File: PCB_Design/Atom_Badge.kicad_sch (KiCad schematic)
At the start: 6 parts

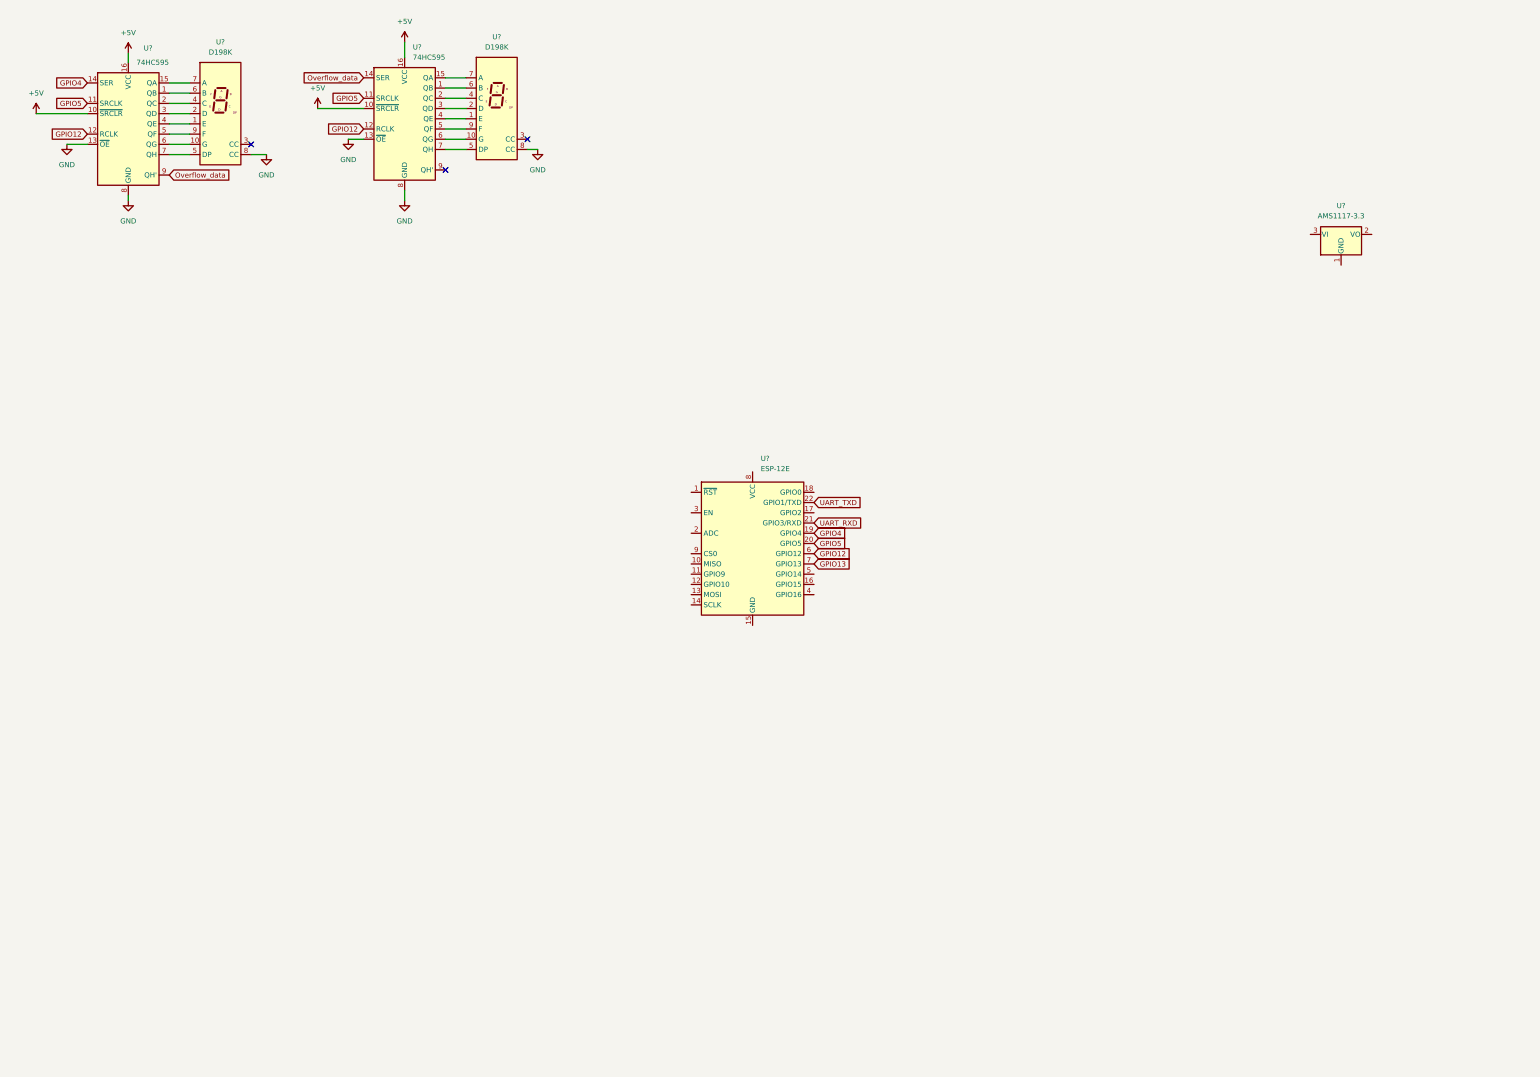
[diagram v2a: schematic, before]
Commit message: added ch340g
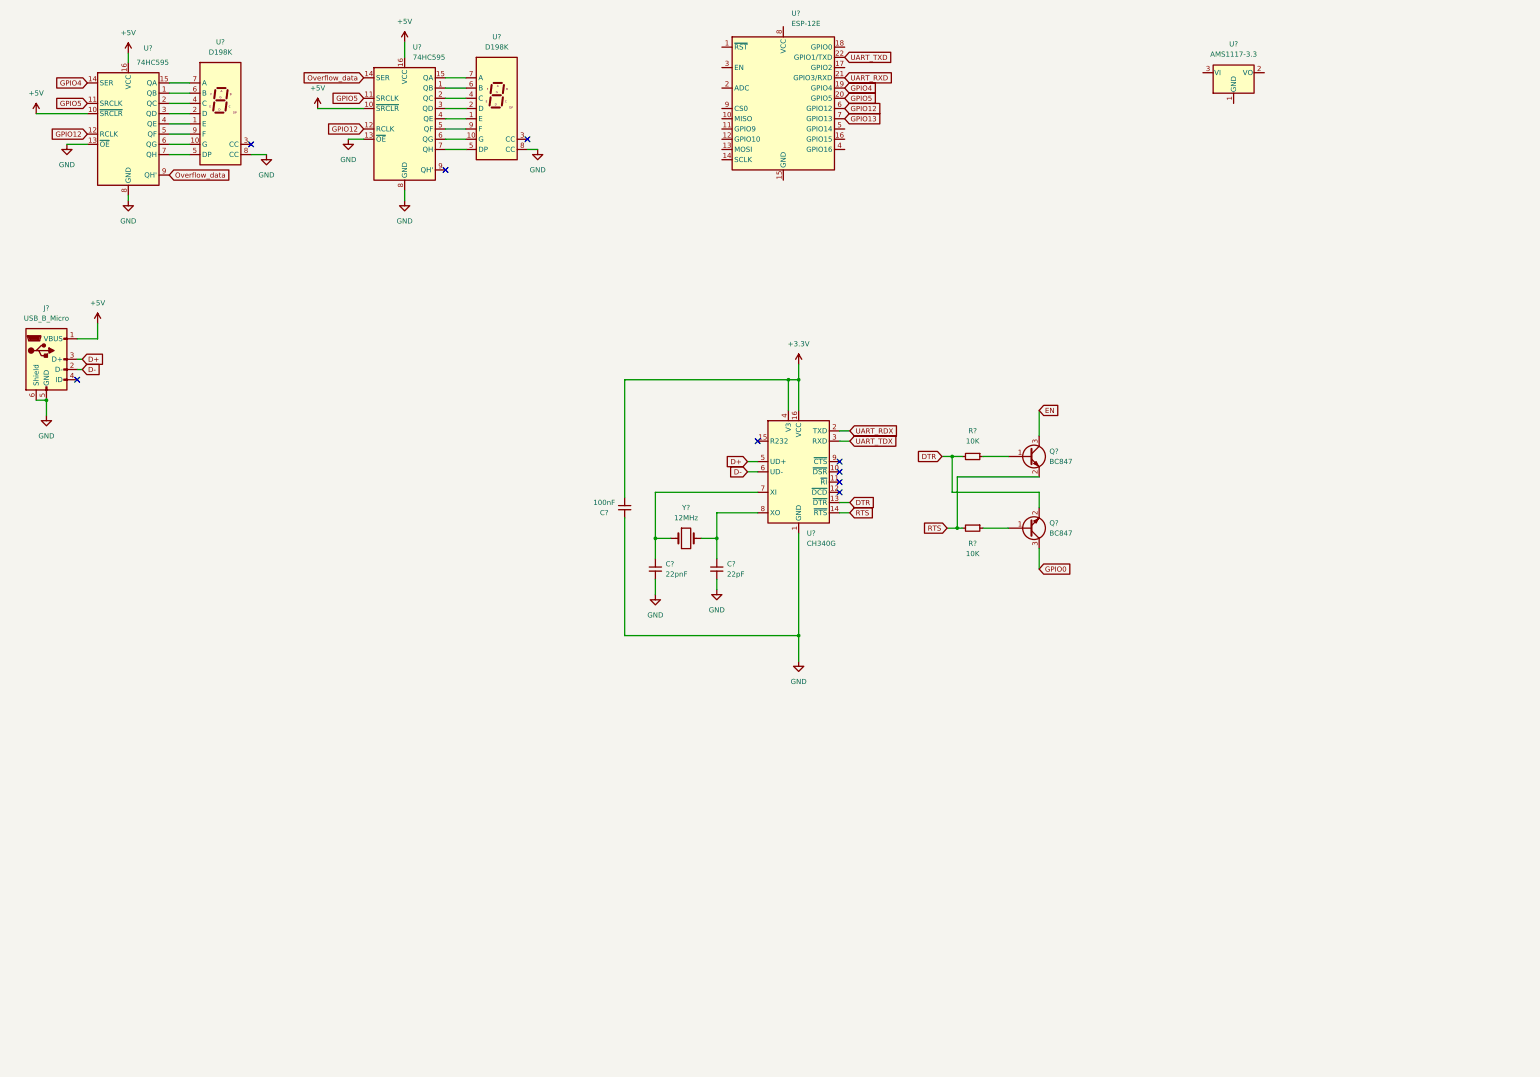
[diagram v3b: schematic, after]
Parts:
- added C?: 22pF, symbol Device:C_Small
- added C?: 100nF, symbol Device:C_Small
- added C?: 22pnF, symbol Device:C_Small
- added J?: USB_B_Micro, symbol Connector:USB_B_Micro
- added Q? (x2): BC847, Package_TO_SOT_SMD:SOT-23, symbol Transistor_BJT:BC847
- added R? (x2): 10K, symbol Device:R_Small
- added U?: CH340G, Package_SO:SOIC-16_3.9x9.9mm_P1.27mm, symbol Interface_USB:CH340G
- added Y?: 12MHz, symbol Device:Crystal
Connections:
- net +5V: now also J?.1 (VBUS)
- net GND: now also C?.2, C?.2, C?.2, J?.5 (GND), J?.6 (Shield), U?.1 (GND)
- new net: Q?.1 (B), R?.1 (x2)
- new net: C?.1, U?.8 (XO), Y?.2
- new net: C?.1, U?.7 (XI), Y?.1
- new net +3V3: C?.1, U?.16 (VCC), U?.4 (V3)
- new net D+: J?.3 (D+), U?.5 (UD+)
- new net D-: J?.2 (D-), U?.6 (UD-)
- new net DTR: Q?.2 (E), R?.2, U?.13 (~{DTR})
- new net EN: Q?.3 (C)
- new net GPIO0: Q?.3 (C)
- new net RTS: Q?.2 (E), R?.2, U?.14 (~{RTS})
- new net UART_RDX: U?.2 (TXD)
- new net UART_TDX: U?.3 (RXD)
- no-connect marks 3 -> 9
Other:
- moved on the sheet: U?

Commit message: Completed 7 segment schematic
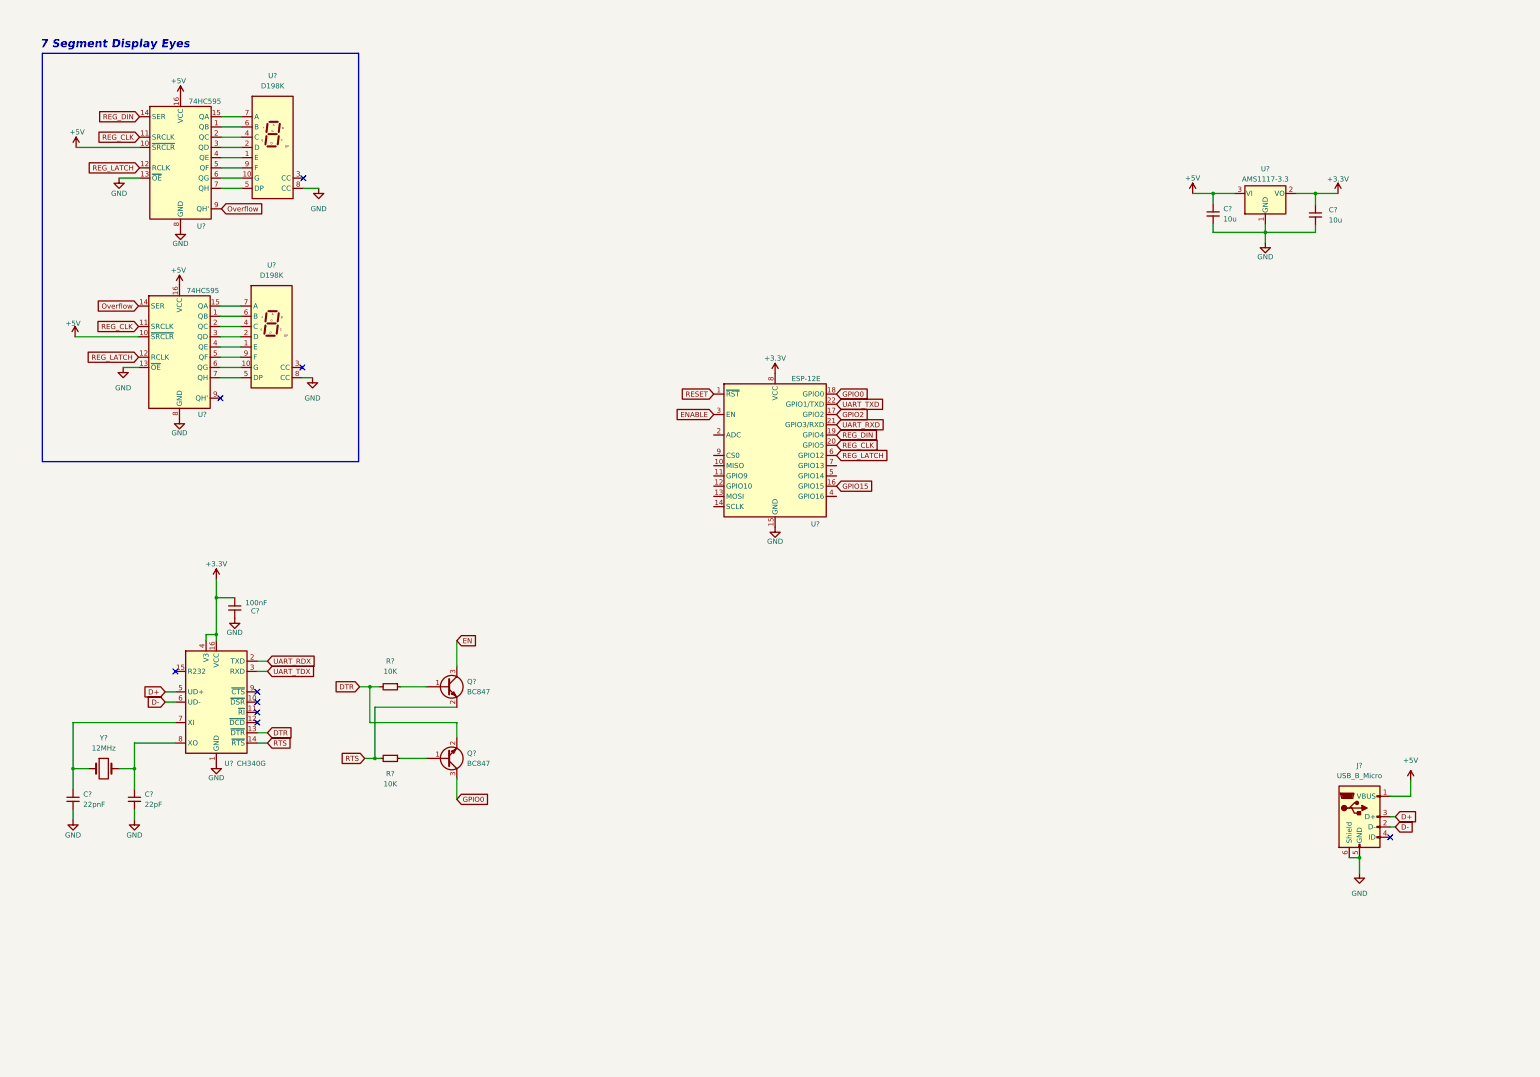
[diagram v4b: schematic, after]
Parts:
- removed C?: 100nF, symbol Device:C_Small
- added C? (x2): 10u, symbol Device:C_Small
- added C?: 100nF, symbol Device:C_Small
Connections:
- net +3V3: now also U?.8 (VCC), C?.1
- net +5V: now also U?.3 (VI), C?.1
- net GND: now also U?.1 (GND), U?.15 (GND), C?.2, C?.2, C?.2
- net GPIO0: now also U?.18 (GPIO0)
- net +3.3V: now reaches U?.2 (VO)
- net +3.3V: now also C?.1
- net RESET: now reaches U?.1 (~{RST})
- net GPIO15: now reaches U?.16 (GPIO15)
- net GPIO2: now reaches U?.17 (GPIO2)
- net ENABLE: now reaches U?.3 (EN)
- net GPIO12 renamed REG_LATCH
- net GPIO13: no longer names the net of U?.7 (GPIO13)
- net GPIO4 renamed REG_DIN
- net GPIO5 renamed REG_CLK
- net Overflow_data renamed Overflow
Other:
- note added: "7 Segment Display Eyes"
- moved on the sheet: C?, J?, Q?, R?, U?, Y?

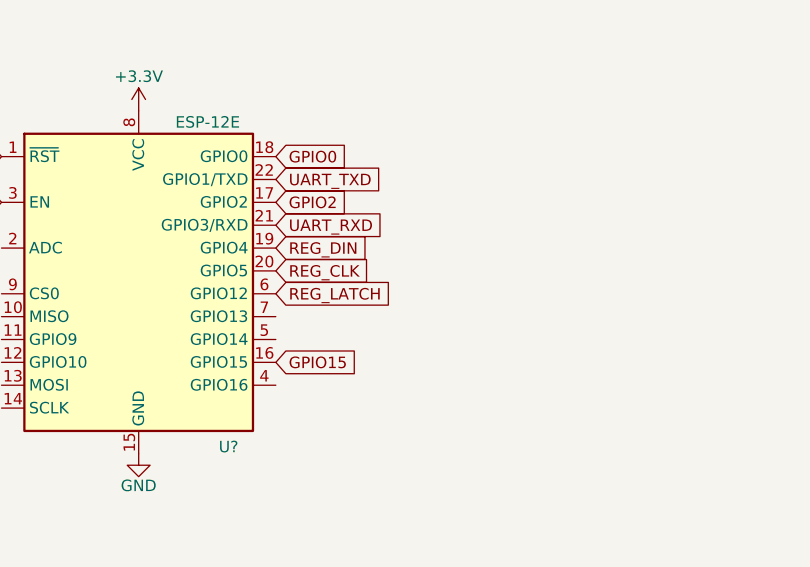
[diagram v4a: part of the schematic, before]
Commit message: Labelled I2C pins
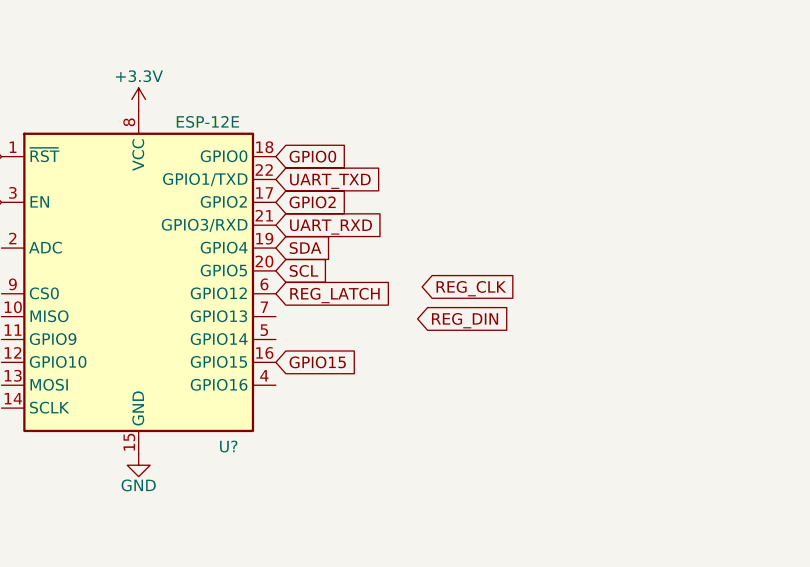
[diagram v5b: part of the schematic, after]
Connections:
- net REG_CLK: no longer U?.20 (GPIO5)
- net REG_DIN: no longer U?.19 (GPIO4)
- new net SCL: U?.20 (GPIO5)
- new net SDA: U?.19 (GPIO4)
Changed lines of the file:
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@@
     (effects (font (size 2 2) (thickness 0.254) bold italic) (justify left bottom))
   )
-  (global_label "REG_DIN" (shape input) (at 222.758 120.396 0) (fields_autoplaced)
+  (global_label "SDA" (shape input) (at 222.758 120.396 0) (fields_autoplaced)
     (effects (font (size 1.27 1.27)) (justify left))
-    (property "Intersheet References" "${INTERSHEET_REFS}" (id 0) (at 233.033 120.4754 0)
+    (property "Intersheet References" "${INTERSHEET_REFS}" (id 0) (at 228.7392 120.3166 0)
+      (effects (font (size 1.27 1.27)) (justify left) hide)
+    )
+  )
+  (global_label "REG_CLK" (shape input) (at 239.014 124.714 0) (fields_autoplaced)
+    (effects (font (size 1.27 1.27)) (justify left))
+    (property "Intersheet References" "${INTERSHEET_REFS}" (id 0) (at 249.6519 124.7934 0)
       (effects (font (size 1.27 1.27)) (justify left) hide)
     )
@@
     (property "Intersheet References" "${INTERSHEET_REFS}" (id 0) (at 182.8497 115.2366 0)
       (effects (font (size 1.27 1.27)) (justify right) hide)
+    )
+  )
+  (global_label "REG_DIN" (shape input) (at 238.506 128.27 0) (fields_autoplaced)
+    (effects (font (size 1.27 1.27)) (justify left))
+    (property "Intersheet References" "${INTERSHEET_REFS}" (id 0) (at 248.781 128.3494 0)
+      (effects (font (size 1.27 1.27)) (justify left) hide)
     )
   )
@@
     )
   )
-  (global_label "REG_CLK" (shape input) (at 222.758 122.936 0) (fields_autoplaced)
+  (global_label "SCL" (shape input) (at 222.758 122.936 0) (fields_autoplaced)
     (effects (font (size 1.27 1.27)) (justify left))
-    (property "Intersheet References" "${INTERSHEET_REFS}" (id 0) (at 233.3959 123.0154 0)
+    (property "Intersheet References" "${INTERSHEET_REFS}" (id 0) (at 228.6787 122.8566 0)
       (effects (font (size 1.27 1.27)) (justify left) hide)
     )

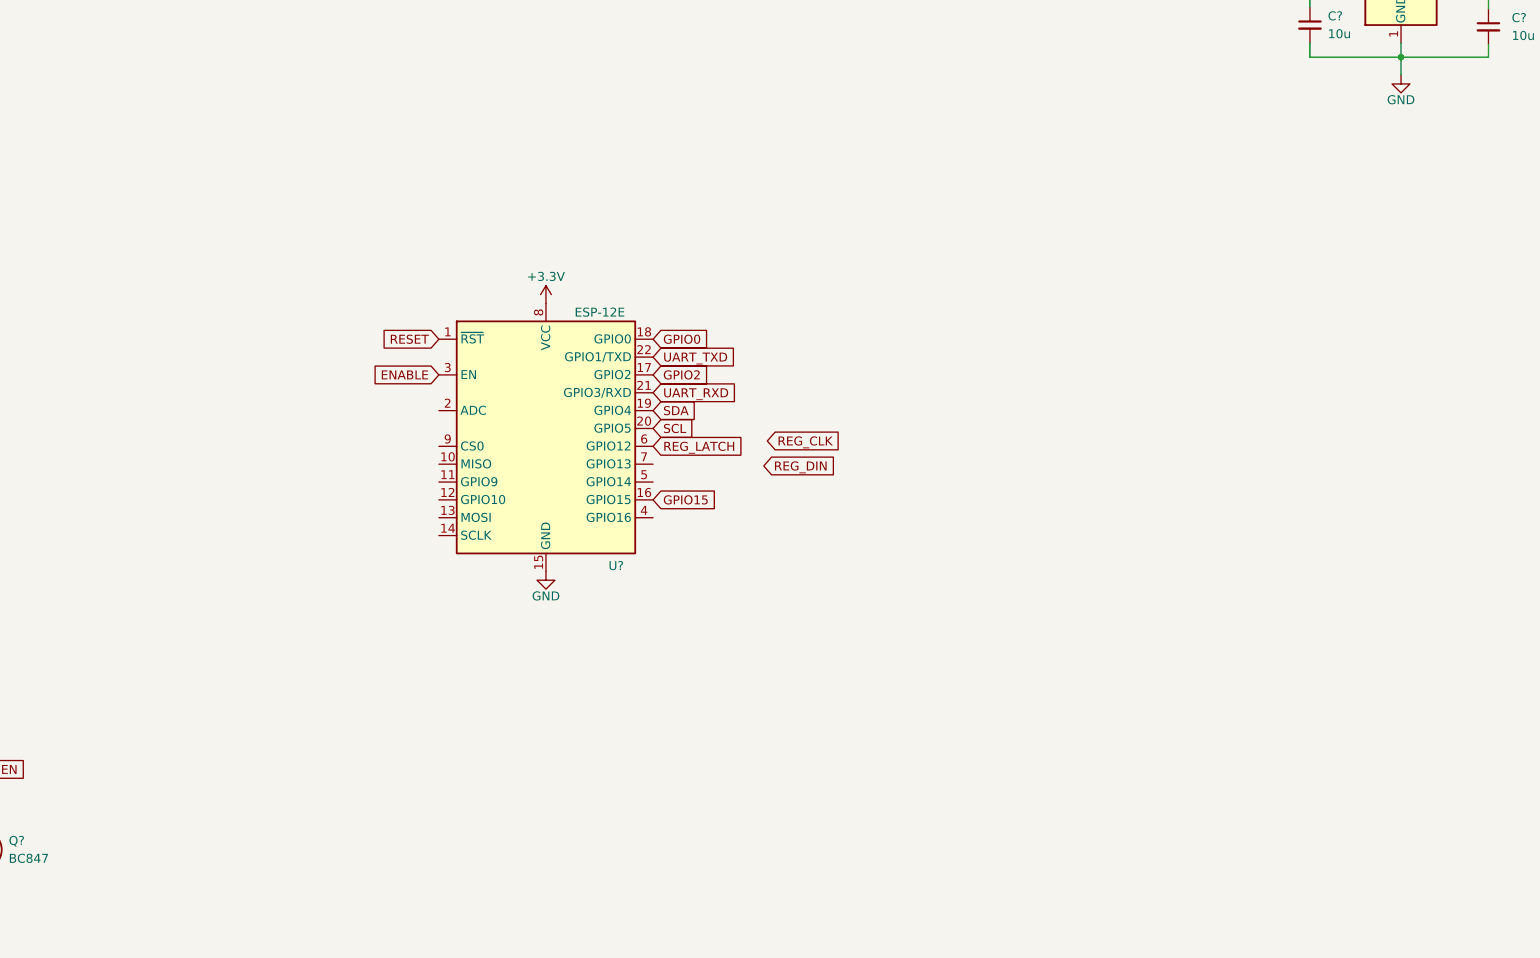
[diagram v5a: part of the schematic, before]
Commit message: transistor model fixed & reset gpio 15 and 2 ckt made
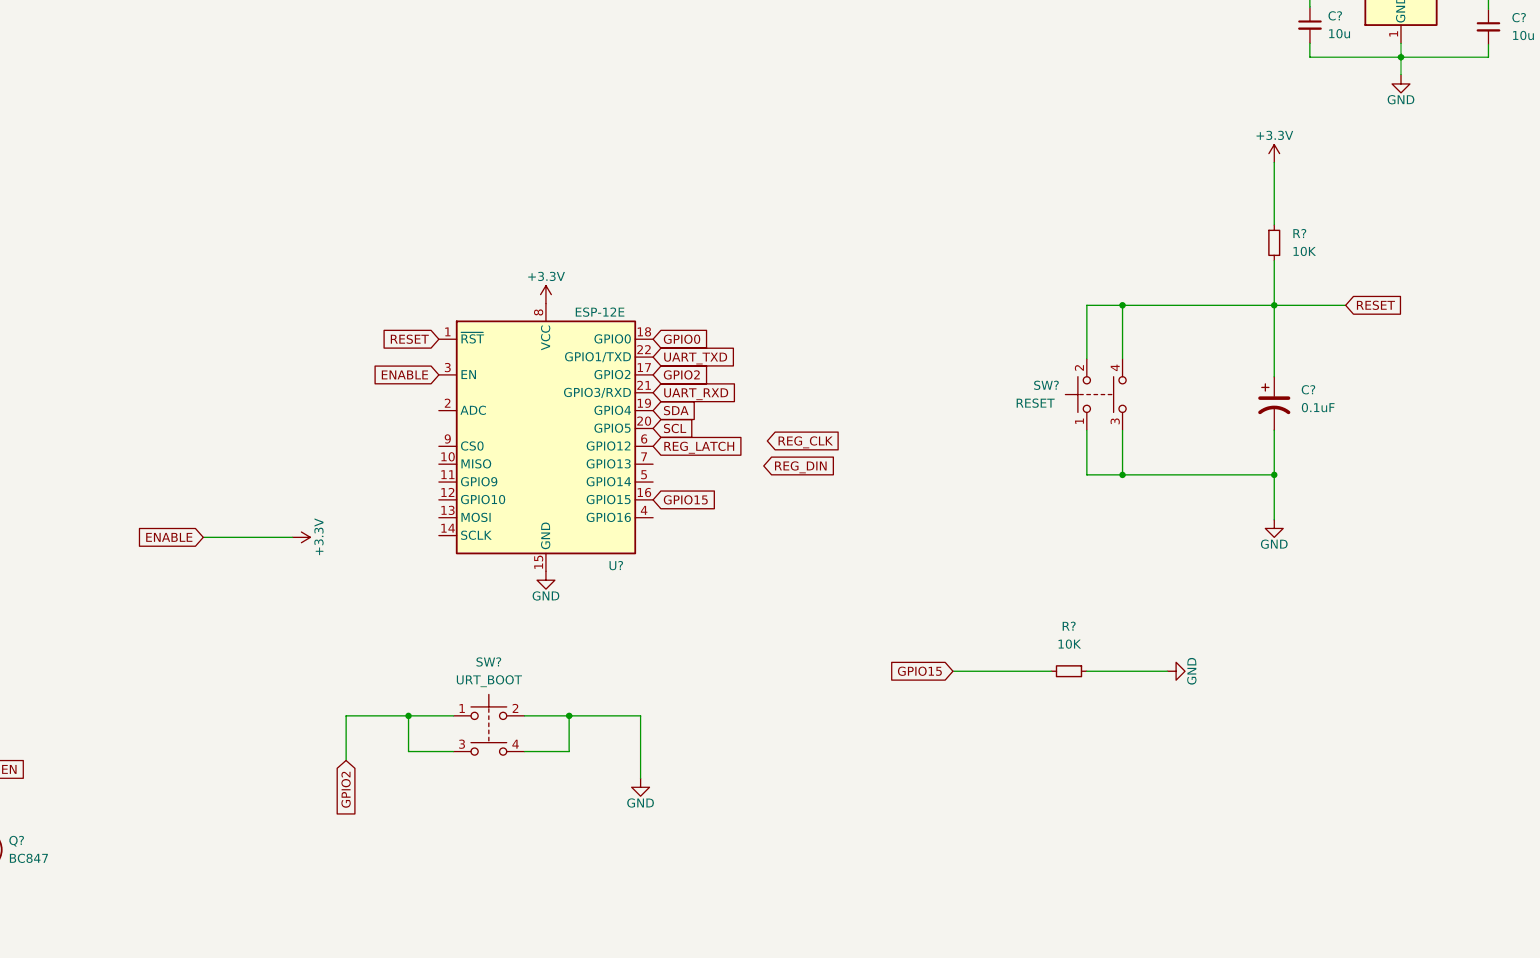
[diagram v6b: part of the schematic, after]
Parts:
- added C?: 0.1uF, symbol Device:C_Polarized_US
- added R? (x2): 10K, symbol Device:R_Small
- added SW?: URT_BOOT, symbol Switch:SW_Push_Dual
- added SW?: RESET, symbol Switch:SW_Push_Dual
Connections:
- net ENABLE is gone; now on net +3V3: U?.3 (EN)
- net +3V3: now also R?.1
- net GND: now also C?.2, R?.1, SW?.1, SW?.2, SW?.3, SW?.4
- net GPIO15: now also R?.2
- net GPIO2: now also SW?.1, SW?.3
- net RESET: now also C?.1, R?.2, SW?.2, SW?.4
